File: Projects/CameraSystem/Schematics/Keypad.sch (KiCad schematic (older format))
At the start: 23 parts, among them J11 Conn_01x06, J12 Conn_01x06, K1 TouchPad, K2 TouchPad, K3 TouchPad, K4 TouchPad, K5 TouchPad, K6 TouchPad, K7 TouchPad, Q3 BC846B_215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

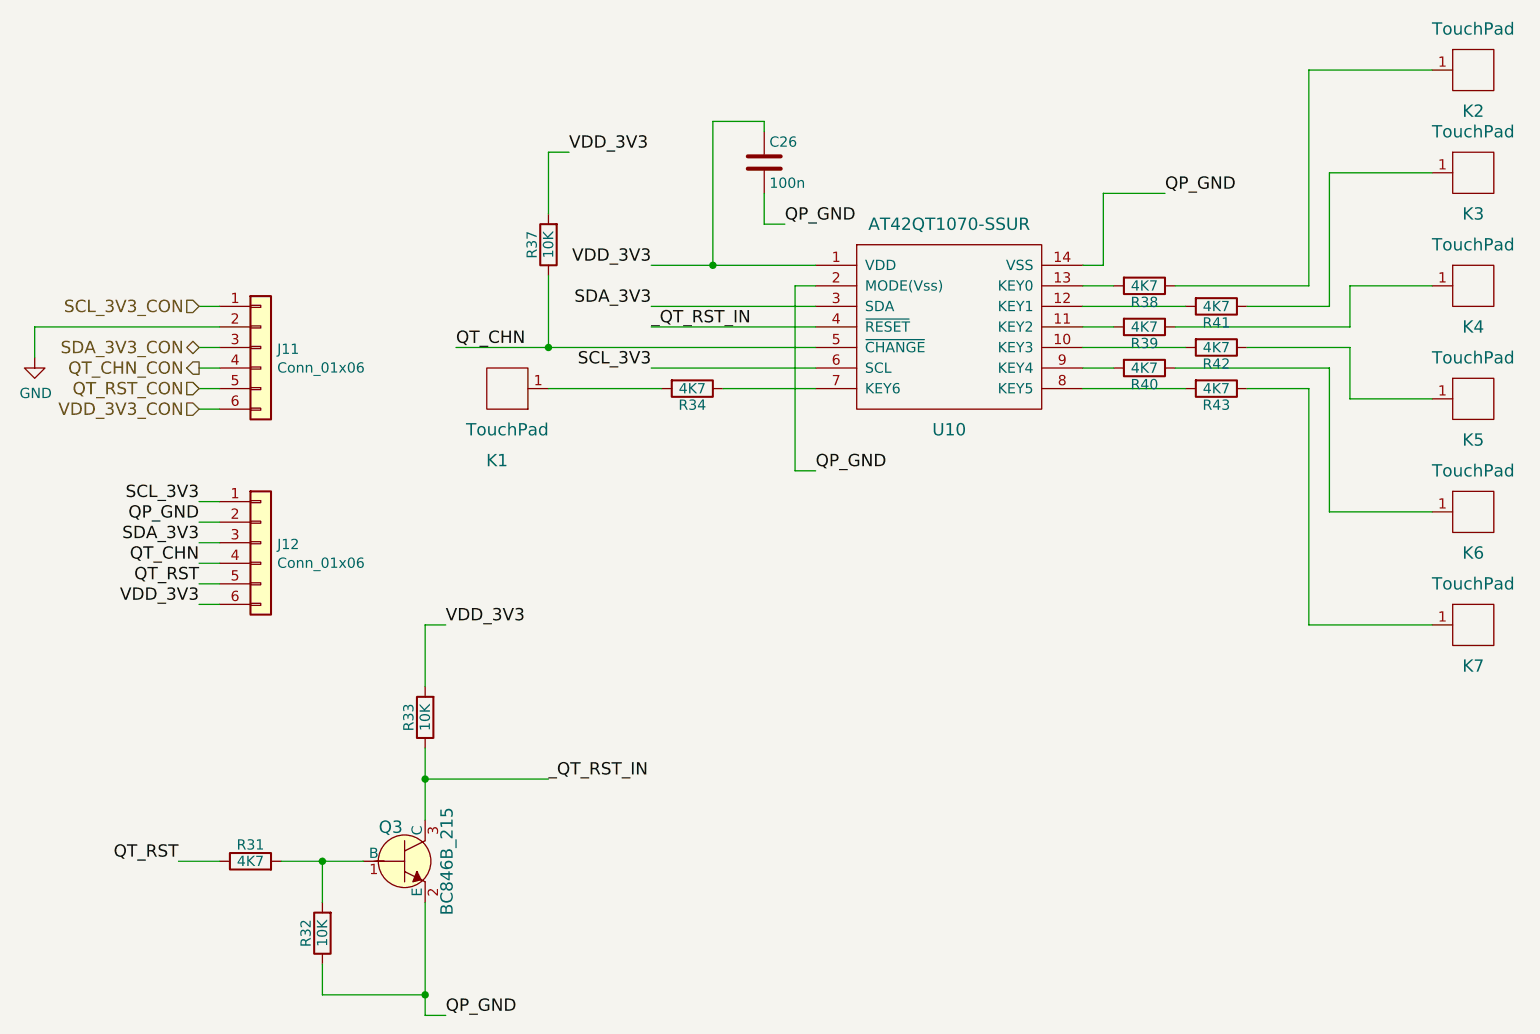
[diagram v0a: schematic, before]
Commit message: camera was updated
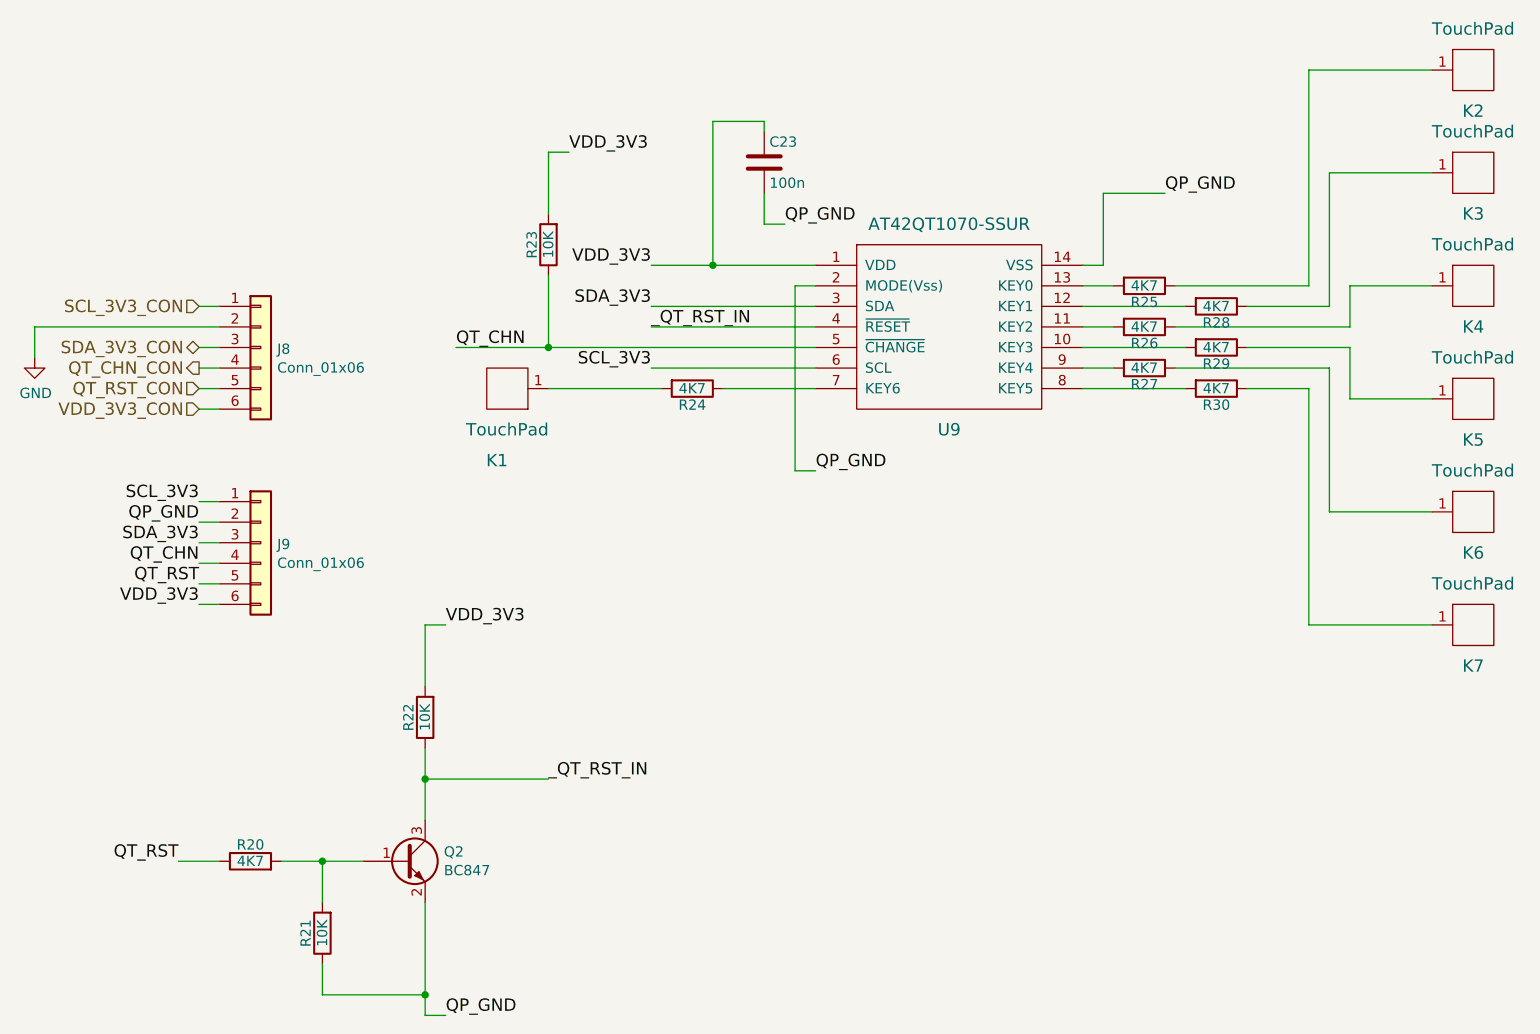
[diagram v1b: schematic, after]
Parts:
- removed Q3: BC846B_215, digikey-footprints:SOT-23-3, symbol CameraSystem-rescue:BC846B_215
- added Q2: BC847, Package_TO_SOT_SMD:SOT-23, symbol Transistor_BJT:BC847
- C23: renamed from C26; footprint digikey-footprints:0603 -> Capacitor_SMD:C_0603_1608Metric_Pad1.05x0.95mm_HandSolder
- J8: renamed from J11; footprint Pin_Headers:Pin_Header_Straight_1x06_Pitch2.54mm -> Connector_PinSocket_2.54mm:PinSocket_1x06_P2.54mm_Vertical
- J9: renamed from J12; footprint Pin_Headers:Pin_Header_Straight_1x06_Pitch2.54mm -> Connector_PinSocket_2.54mm:PinSocket_1x06_P2.54mm_Vertical
- R20: renamed from R31; footprint digikey-footprints:0603 -> Resistor_SMD:R_0603_1608Metric_Pad1.05x0.95mm_HandSolder
- R21: renamed from R32; footprint digikey-footprints:0603 -> Resistor_SMD:R_0603_1608Metric_Pad1.05x0.95mm_HandSolder
- R22: renamed from R33; footprint digikey-footprints:0603 -> Resistor_SMD:R_0603_1608Metric_Pad1.05x0.95mm_HandSolder
- R23: renamed from R37; footprint digikey-footprints:0603 -> Resistor_SMD:R_0603_1608Metric_Pad1.05x0.95mm_HandSolder
- R24: renamed from R34; footprint digikey-footprints:0603 -> Resistor_SMD:R_0603_1608Metric_Pad1.05x0.95mm_HandSolder
- R25: renamed from R38; footprint digikey-footprints:0603 -> Resistor_SMD:R_0603_1608Metric_Pad1.05x0.95mm_HandSolder
- R26: renamed from R39; footprint digikey-footprints:0603 -> Resistor_SMD:R_0603_1608Metric_Pad1.05x0.95mm_HandSolder
- R27: renamed from R40; footprint digikey-footprints:0603 -> Resistor_SMD:R_0603_1608Metric_Pad1.05x0.95mm_HandSolder
- R28: renamed from R41; footprint digikey-footprints:0603 -> Resistor_SMD:R_0603_1608Metric_Pad1.05x0.95mm_HandSolder
- R29: renamed from R42; footprint digikey-footprints:0603 -> Resistor_SMD:R_0603_1608Metric_Pad1.05x0.95mm_HandSolder
- R30: renamed from R43; footprint digikey-footprints:0603 -> Resistor_SMD:R_0603_1608Metric_Pad1.05x0.95mm_HandSolder
- renumbered U10 to U9
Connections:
- net QP_GND: now also Q2.2 (E)
- net _QT_RST_IN: now also Q2.3 (C)
- net at R20.2, R21.2: now also Q2.1 (B)
